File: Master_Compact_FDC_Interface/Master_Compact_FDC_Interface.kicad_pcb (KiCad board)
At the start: 2 copper layers, 25.7 x 53.1 mm, 2 parts, among them J1 BBC Master Compact, J2 Gotek

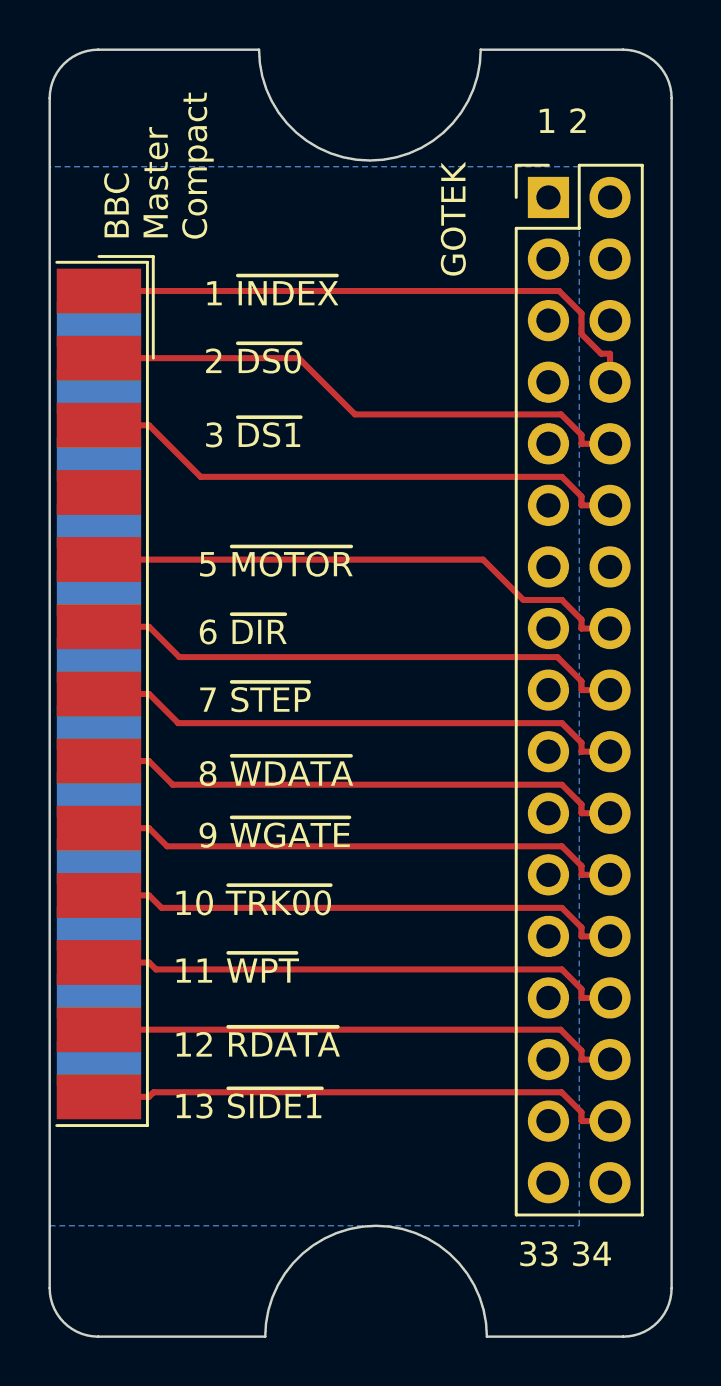
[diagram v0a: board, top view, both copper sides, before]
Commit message: Reversed IDC header
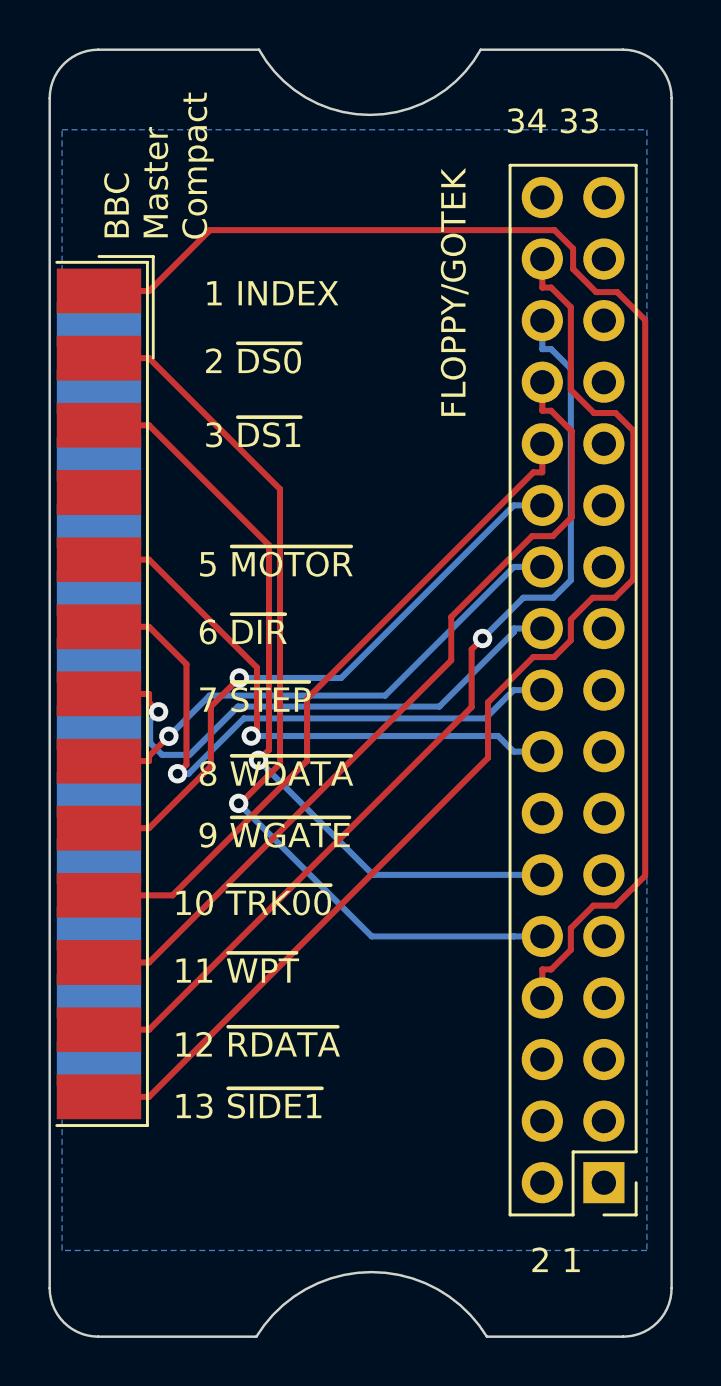
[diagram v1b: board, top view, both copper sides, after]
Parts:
- moved J2 40.7 mm to (119.1, 89.7), turned to 180 degrees
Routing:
- net ~{INDEX}: track 23.8 -> 56.1 mm
- net ~{SIDE1}: track 21.9 -> 48.2 mm
- net ~{RDATA}: track 21.8 -> 39.9 mm, vias 0 -> 1
- net ~{DS0}: track 22.8 -> 38.2 mm, vias 0 -> 1
- net ~{WPT}: track 21.9 -> 34.4 mm
- net ~{DS1}: track 22.7 -> 31.8 mm, vias 0 -> 1
- net ~{TRK00}: track 22.0 -> 28.2 mm
- net ~{WGATE}: track 22.1 -> 25.3 mm, vias 0 -> 1
- net ~{DIR}: track 22.4 -> 25.4 mm, vias 0 -> 1
- net ~{MOTOR}: track 22.5 -> 23.6 mm, vias 0 -> 1
- net ~{STEP}: track 22.3 -> 23.0 mm, vias 0 -> 1
- net ~{WDATA}: track 22.2 -> 21.7 mm, vias 0 -> 1
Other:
- outline, holes or cut-outs redrawn
- board text added: "1 INDEX"
- board text added: "2 1"
- board text added: "34 33"
- board text added: "FLOPPY/GOTEK"
- board text removed: "1 2"
- board text removed: "1 ~{INDEX}"
- board text removed: "33 34"
- board text removed: "GOTEK"

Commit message: Added "schematic scraps" section
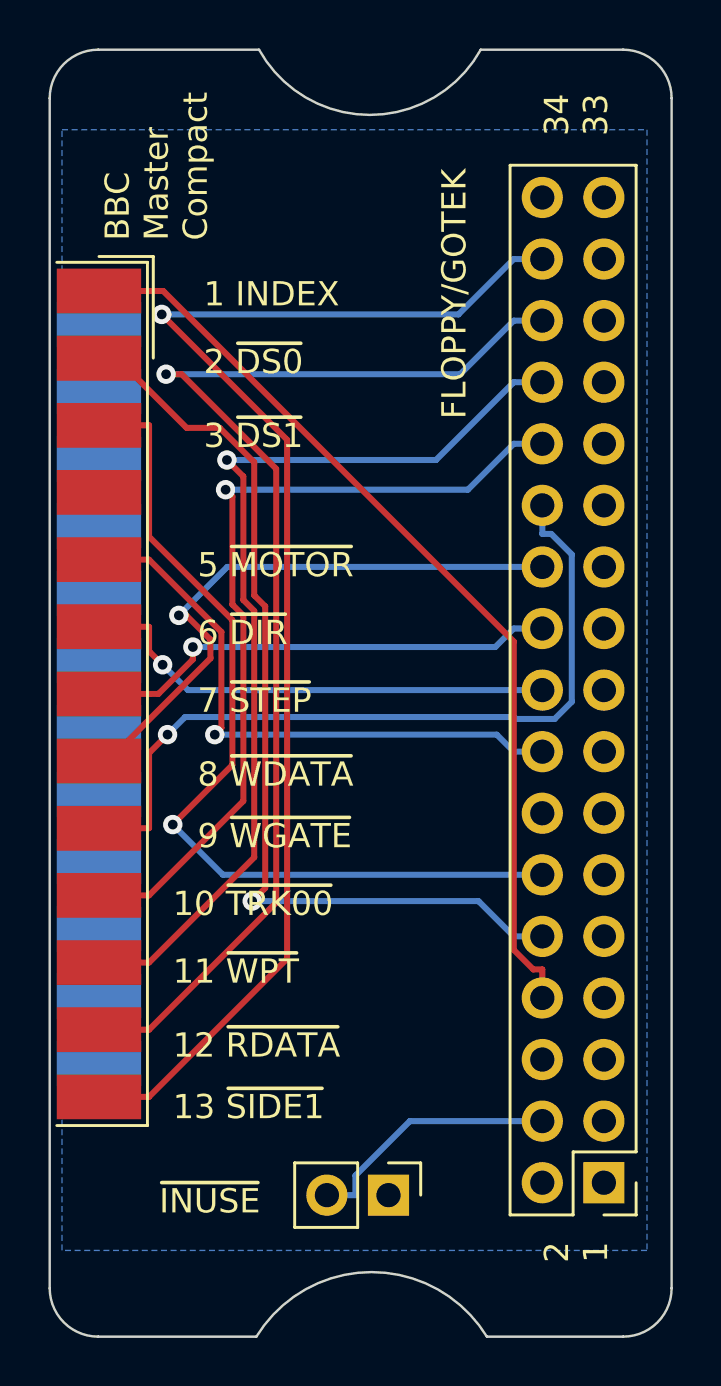
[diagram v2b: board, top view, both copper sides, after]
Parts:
- added J3: ~{INUSE}, Connector_PinHeader_2.54mm:PinHeader_1x02_P2.54mm_Vertical, F.Cu at (110.2, 90.2)
- J1: value BBC Master Compact -> BBC
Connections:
- net ~{INDEX} renamed INDEX
- J2 pad 4: unconnected-(J2-Pin_4-Pad4) -> Net-(J2-Pin_4)
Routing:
- net INDEX: track 56.1 -> 38.5 mm
- net Net-(J2-Pin_4): track 0.00 -> 10.6 mm
- net ~{RDATA}: track 39.9 -> 50.0 mm
- net ~{SIDE1}: track 48.2 -> 55.5 mm, vias 0 -> 1
- net ~{WGATE}: track 25.3 -> 32.4 mm
- net ~{TRK00}: track 28.2 -> 34.6 mm, vias 0 -> 1
- net ~{DIR}: track 25.4 -> 20.0 mm
- net ~{DS1}: track 31.8 -> 37.1 mm
- net ~{WPT}: track 34.4 -> 39.4 mm, vias 0 -> 1
- net ~{STEP}: track 23.0 -> 19.7 mm
- net ~{WDATA}: track 21.7 -> 24.7 mm
- net ~{DS0}: track 38.2 -> 39.3 mm
- net ~{MOTOR}: track 23.6 -> 24.4 mm
